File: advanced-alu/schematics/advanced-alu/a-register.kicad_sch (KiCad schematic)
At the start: 10 parts, among them U10 74LS194, U3 74LS04, U4 74LS08, U5 74LS245, U6 74LS32, U7 74LS86, U8 74LS08, U9 74LS194

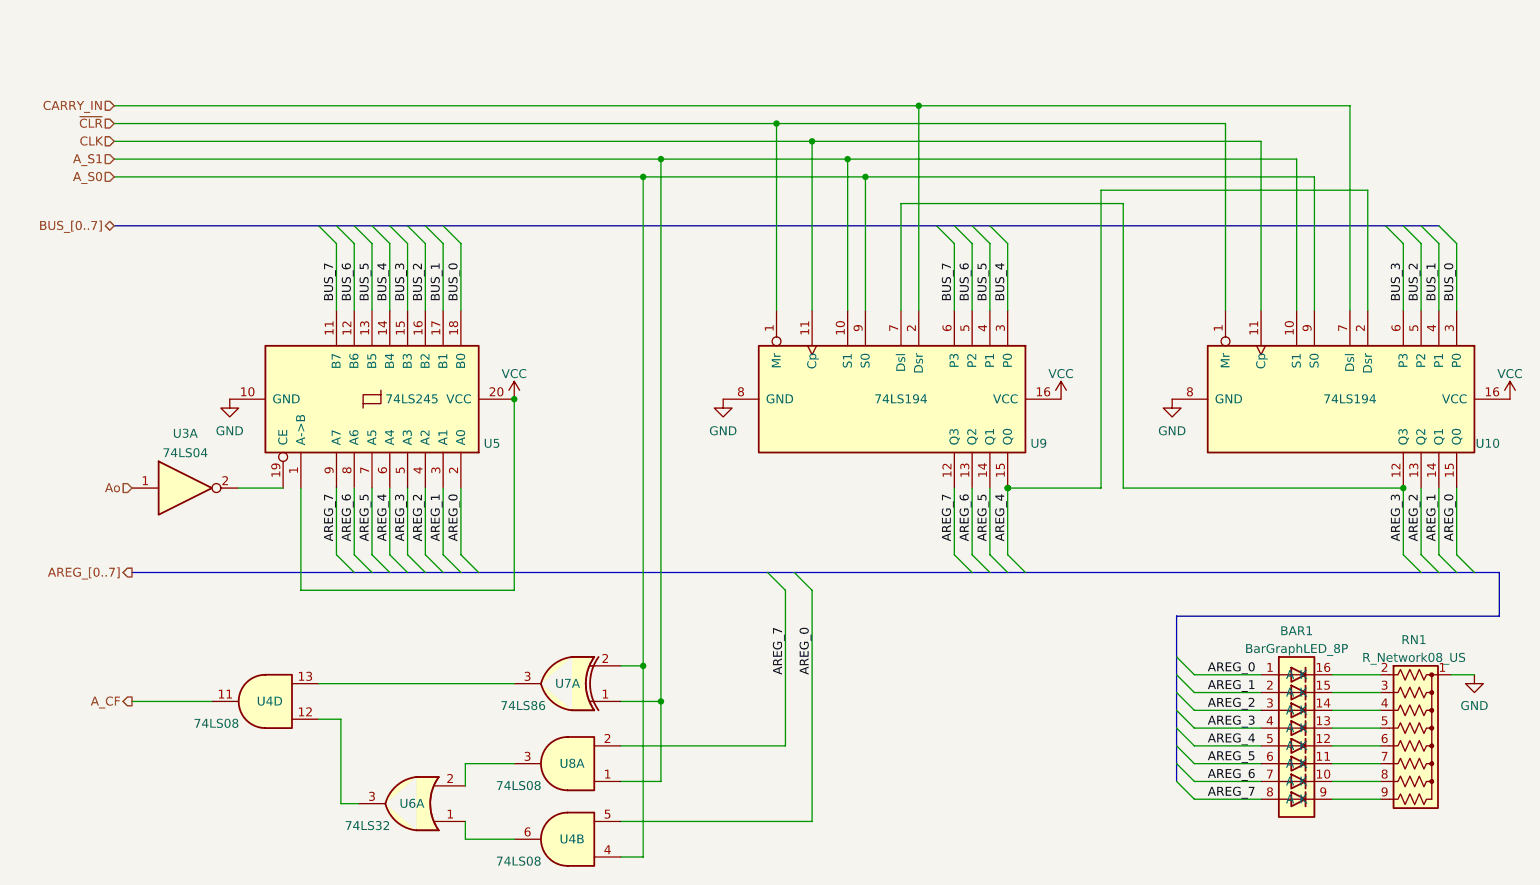
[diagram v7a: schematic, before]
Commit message: fixed bit shifting hardware bug
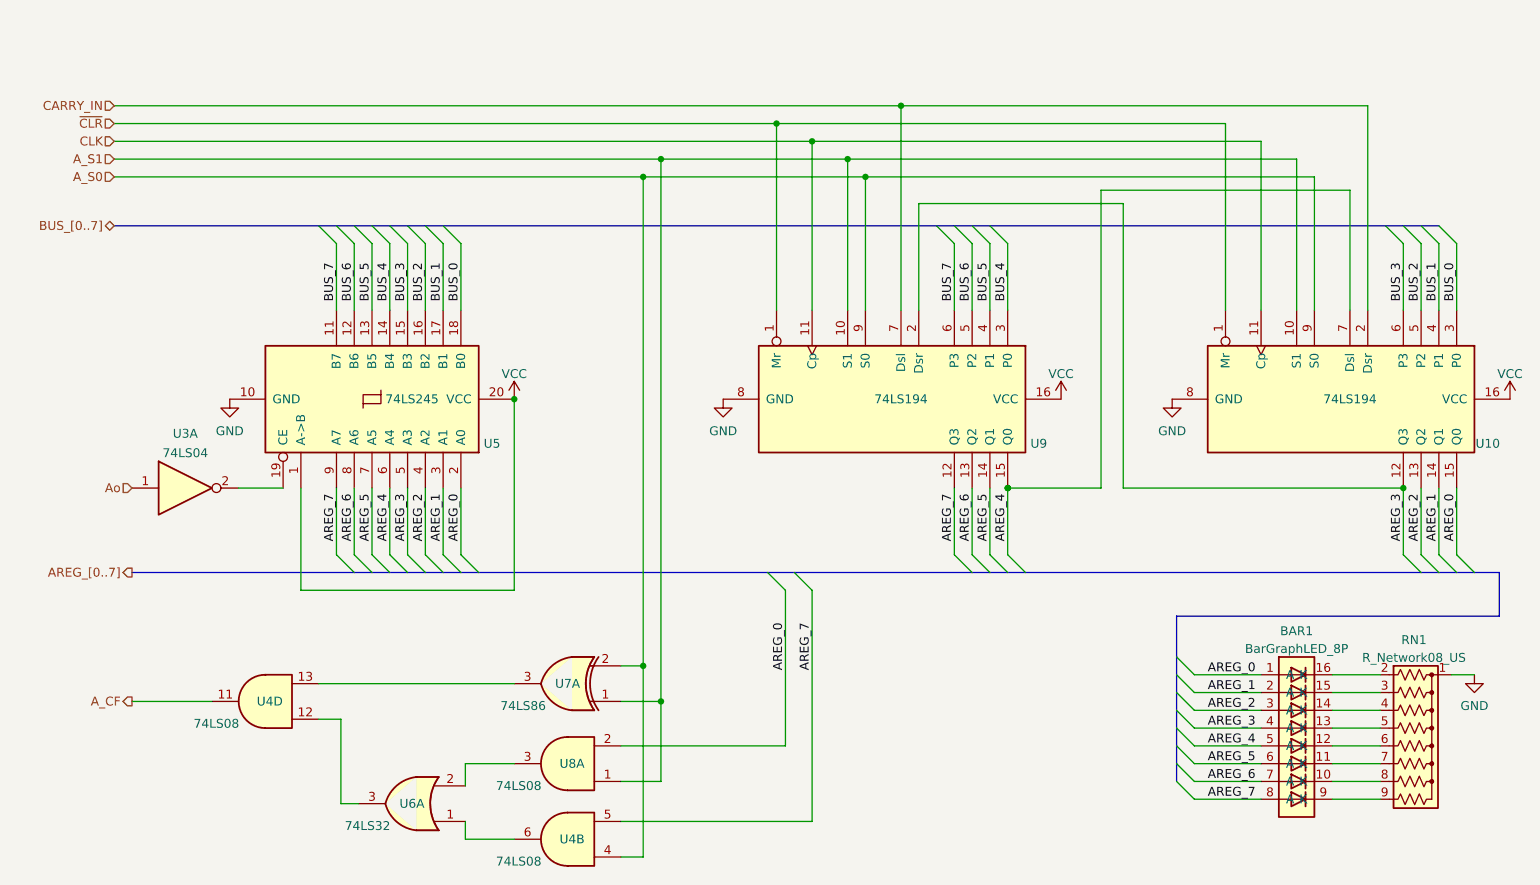
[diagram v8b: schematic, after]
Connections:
- net AREG_0: now also U8.2; no longer U4.5
- net AREG_3: now also U9.2 (Dsr); no longer U9.7 (Dsl)
- net AREG_4: now also U10.7 (Dsl); no longer U10.2 (Dsr)
- net AREG_7: now also U4.5; no longer U8.2
- net CARRY_IN: now also U10.2 (Dsr), U9.7 (Dsl); no longer U10.7 (Dsl), U9.2 (Dsr)
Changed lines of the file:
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@@
   (title_block
     (title "Advanced Arithmetic Logic Unit - Accumulator/Shifter")
+    (comment 2 "A_S0, A_S1 loads A from data bus")
+    (comment 3 "~{A_S0}, A_S1 is right shift")
+    (comment 4 "A_S0, ~{A_S1} is left shift")
+  )
+  (junction (at 127.635 132.08) (diameter 0) (color 0 0 0 0)
+  )
+  (junction (at 164.465 52.07) (diameter 0) (color 0 0 0 0)
   )
   (junction (at 179.7246 106.68) (diameter 0) (color 0 0 0 0)
@@
   (junction (at 146.685 54.61) (diameter 0) (color 0 0 0 0)
   )
+  (junction (at 179.705 106.68) (diameter 0) (color 0 0 0 0)
+  )
+  (junction (at 159.385 62.23) (diameter 0) (color 0 0 0 0)
+  )
+  (junction (at 151.765 57.15) (diameter 0) (color 0 0 0 0)
+  )
+  (junction (at 127.635 62.23) (diameter 0) (color 0 0 0 0)
+  )
+  (junction (at 109.22 93.98) (diameter 0) (color 0 0 0 0)
+  )
   (junction (at 130.175 137.16) (diameter 0) (color 0 0 0 0)
   )
-  (junction (at 179.705 106.68) (diameter 0) (color 0 0 0 0)
-  )
-  (junction (at 159.385 62.23) (diameter 0) (color 0 0 0 0)
-  )
-  (junction (at 127.635 132.08) (diameter 0) (color 0 0 0 0)
-  )
-  (junction (at 151.765 57.15) (diameter 0) (color 0 0 0 0)
-  )
-  (junction (at 127.635 62.23) (diameter 0) (color 0 0 0 0)
-  )
-  (junction (at 109.22 93.98) (diameter 0) (color 0 0 0 0)
-  )
-  (junction (at 167.005 52.07) (diameter 0) (color 0 0 0 0)
-  )
   (junction (at 236.22 106.68) (diameter 0) (color 0 0 0 0)
   )
@@
     (stroke (width 0) (type default) (color 0 0 0 0))
   )
+  (wire (pts (xy 167.005 66.04) (xy 167.005 81.28))
+    (stroke (width 0) (type default) (color 0 0 0 0))
+  )
   (wire (pts (xy 147.955 121.285) (xy 147.955 143.51))
     (stroke (width 0) (type default) (color 0 0 0 0))
@@
     (stroke (width 0) (type default) (color 0 0 0 0))
   )
-  (wire (pts (xy 164.465 66.04) (xy 164.465 81.28))
-    (stroke (width 0) (type default) (color 0 0 0 0))
-  )
   (bus (pts (xy 91.44 118.745) (xy 93.98 118.745))
     (stroke (width 0) (type default) (color 0 0 0 0))
@@
     (stroke (width 0) (type default) (color 0 0 0 0))
   )
+  (wire (pts (xy 193.04 64.135) (xy 228.6 64.135))
+    (stroke (width 0) (type default) (color 0 0 0 0))
+  )
   (wire (pts (xy 215.9 138.43) (xy 206.375 138.43))
     (stroke (width 0) (type default) (color 0 0 0 0))
@@
     (stroke (width 0) (type default) (color 0 0 0 0))
   )
+  (wire (pts (xy 127.635 159.385) (xy 124.46 159.385))
+    (stroke (width 0) (type default) (color 0 0 0 0))
+  )
   (bus (pts (xy 91.44 69.215) (xy 93.98 69.215))
     (stroke (width 0) (type default) (color 0 0 0 0))
   )
-  (wire (pts (xy 228.6 81.28) (xy 228.6 52.07))
-    (stroke (width 0) (type default) (color 0 0 0 0))
-  )
   (wire (pts (xy 99.06 71.755) (xy 99.06 81.28))
     (stroke (width 0) (type default) (color 0 0 0 0))
@@
     (stroke (width 0) (type default) (color 0 0 0 0))
   )
+  (wire (pts (xy 228.6 64.135) (xy 228.6 81.28))
+    (stroke (width 0) (type default) (color 0 0 0 0))
+  )
   (bus (pts (xy 169.545 69.215) (xy 172.085 69.215))
     (stroke (width 0) (type default) (color 0 0 0 0))
@@
     (stroke (width 0) (type default) (color 0 0 0 0))
   )
+  (wire (pts (xy 164.465 52.07) (xy 164.465 81.28))
+    (stroke (width 0) (type default) (color 0 0 0 0))
+  )
   (wire (pts (xy 83.82 71.755) (xy 83.82 81.28))
     (stroke (width 0) (type default) (color 0 0 0 0))
@@
     (stroke (width 0) (type default) (color 0 0 0 0))
   )
-  (wire (pts (xy 130.175 148.59) (xy 130.175 137.16))
-    (stroke (width 0) (type default) (color 0 0 0 0))
-  )
   (wire (pts (xy 241.3 71.755) (xy 241.3 81.28))
     (stroke (width 0) (type default) (color 0 0 0 0))
@@
     (stroke (width 0) (type default) (color 0 0 0 0))
   )
-  (wire (pts (xy 127.635 159.385) (xy 124.46 159.385))
-    (stroke (width 0) (type default) (color 0 0 0 0))
-  )
   (wire (pts (xy 210.82 81.28) (xy 210.82 54.61))
     (stroke (width 0) (type default) (color 0 0 0 0))
@@
     (stroke (width 0) (type default) (color 0 0 0 0))
   )
-  (wire (pts (xy 167.005 52.07) (xy 228.6 52.07))
-    (stroke (width 0) (type default) (color 0 0 0 0))
-  )
-  (wire (pts (xy 193.04 64.135) (xy 231.14 64.135))
-    (stroke (width 0) (type default) (color 0 0 0 0))
-  )
   (bus (pts (xy 96.52 118.745) (xy 99.06 118.745))
     (stroke (width 0) (type default) (color 0 0 0 0))
@@
     (stroke (width 0) (type default) (color 0 0 0 0))
   )
-  (wire (pts (xy 231.14 64.135) (xy 231.14 81.28))
-    (stroke (width 0) (type default) (color 0 0 0 0))
-  )
   (wire (pts (xy 88.9 106.68) (xy 88.9 116.205))
     (stroke (width 0) (type default) (color 0 0 0 0))
@@
     (stroke (width 0) (type default) (color 0 0 0 0))
   )
+  (wire (pts (xy 130.175 137.16) (xy 130.175 148.59))
+    (stroke (width 0) (type default) (color 0 0 0 0))
+  )
+  (wire (pts (xy 179.705 106.68) (xy 179.7246 106.68))
+    (stroke (width 0) (type default) (color 0 0 0 0))
+  )
+  (wire (pts (xy 83.82 106.68) (xy 83.82 116.205))
+    (stroke (width 0) (type default) (color 0 0 0 0))
+  )
+  (bus (pts (xy 93.98 118.745) (xy 96.52 118.745))
+    (stroke (width 0) (type default) (color 0 0 0 0))
+  )
+  (bus (pts (xy 86.36 118.745) (xy 88.9 118.745))
+    (stroke (width 0) (type default) (color 0 0 0 0))
+  )
+  (wire (pts (xy 91.44 106.68) (xy 91.44 116.205))
+    (stroke (width 0) (type default) (color 0 0 0 0))
+  )
+  (wire (pts (xy 84.455 151.765) (xy 84.455 139.7))
+    (stroke (width 0) (type default) (color 0 0 0 0))
+  )
+  (wire (pts (xy 130.175 148.59) (xy 124.46 148.59))
+    (stroke (width 0) (type default) (color 0 0 0 0))
+  )
+  (wire (pts (xy 172.085 106.68) (xy 172.085 116.205))
+    (stroke (width 0) (type default) (color 0 0 0 0))
+  )
   (wire (pts (xy 127.635 132.08) (xy 127.635 159.385))
     (stroke (width 0) (type default) (color 0 0 0 0))
   )
-  (wire (pts (xy 179.705 106.68) (xy 179.7246 106.68))
-    (stroke (width 0) (type default) (color 0 0 0 0))
-  )
-  (wire (pts (xy 83.82 106.68) (xy 83.82 116.205))
-    (stroke (width 0) (type default) (color 0 0 0 0))
-  )
-  (bus (pts (xy 93.98 118.745) (xy 96.52 118.745))
-    (stroke (width 0) (type default) (color 0 0 0 0))
-  )
-  (bus (pts (xy 86.36 118.745) (xy 88.9 118.745))
-    (stroke (width 0) (type default) (color 0 0 0 0))
-  )
-  (wire (pts (xy 91.44 106.68) (xy 91.44 116.205))
-    (stroke (width 0) (type default) (color 0 0 0 0))
-  )
-  (wire (pts (xy 84.455 151.765) (xy 84.455 139.7))
-    (stroke (width 0) (type default) (color 0 0 0 0))
-  )
-  (wire (pts (xy 172.085 106.68) (xy 172.085 116.205))
-    (stroke (width 0) (type default) (color 0 0 0 0))
-  )
   (bus (pts (xy 243.84 118.745) (xy 246.38 118.745))
     (stroke (width 0) (type default) (color 0 0 0 0))
@@
     (stroke (width 0) (type default) (color 0 0 0 0))
   )
+  (wire (pts (xy 231.14 81.28) (xy 231.14 52.07))
+    (stroke (width 0) (type default) (color 0 0 0 0))
+  )
   (bus (pts (xy 177.165 69.215) (xy 233.68 69.215))
     (stroke (width 0) (type default) (color 0 0 0 0))
@@
     (stroke (width 0) (type default) (color 0 0 0 0))
   )
-  (wire (pts (xy 124.46 148.59) (xy 130.175 148.59))
-    (stroke (width 0) (type default) (color 0 0 0 0))
-  )
   (bus (pts (xy 203.835 148.59) (xy 203.835 146.05))
     (stroke (width 0) (type default) (color 0 0 0 0))
@@
     (stroke (width 0) (type default) (color 0 0 0 0))
   )
-  (wire (pts (xy 52.07 52.07) (xy 167.005 52.07))
+  (wire (pts (xy 52.07 52.07) (xy 164.465 52.07))
     (stroke (width 0) (type default) (color 0 0 0 0))
   )
@@
     (stroke (width 0) (type default) (color 0 0 0 0))
   )
-  (wire (pts (xy 196.215 66.04) (xy 164.465 66.04))
-    (stroke (width 0) (type default) (color 0 0 0 0))
-  )
   (bus (pts (xy 241.3 118.745) (xy 243.84 118.745))
     (stroke (width 0) (type default) (color 0 0 0 0))
@@
     (stroke (width 0) (type default) (color 0 0 0 0))
   )
-  (wire (pts (xy 167.005 52.07) (xy 167.005 81.28))
-    (stroke (width 0) (type default) (color 0 0 0 0))
-  )
   (wire (pts (xy 223.52 81.28) (xy 223.52 62.23))
     (stroke (width 0) (type default) (color 0 0 0 0))
@@
     (stroke (width 0) (type default) (color 0 0 0 0))
   )
+  (wire (pts (xy 196.215 66.04) (xy 167.005 66.04))
+    (stroke (width 0) (type default) (color 0 0 0 0))
+  )
   (wire (pts (xy 196.215 106.68) (xy 196.215 66.04))
     (stroke (width 0) (type default) (color 0 0 0 0))
@@
     (stroke (width 0) (type default) (color 0 0 0 0))
   )
+  (wire (pts (xy 164.465 52.07) (xy 231.14 52.07))
+    (stroke (width 0) (type default) (color 0 0 0 0))
+  )
   (wire (pts (xy 130.175 59.69) (xy 156.845 59.69))
     (stroke (width 0) (type default) (color 0 0 0 0))
@@
     (effects (font (size 1.27 1.27)) (justify left bottom))
   )
-  (label "AREG_7" (at 147.955 133.35 90)
+  (label "AREG_7" (at 151.765 132.715 90)
     (effects (font (size 1.27 1.27)) (justify left bottom))
   )
@@
     (effects (font (size 1.27 1.27)) (justify left bottom))
   )
-  (label "AREG_0" (at 151.765 133.35 90)
-    (effects (font (size 1.27 1.27)) (justify left bottom))
-  )
+  (label "AREG_0" (at 147.955 132.715 90)
+    (effects (font (size 1.27 1.27)) (justify left bottom))
+  )
